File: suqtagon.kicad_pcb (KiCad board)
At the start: 2 copper layers, 100 x 86.6 mm, 2 parts

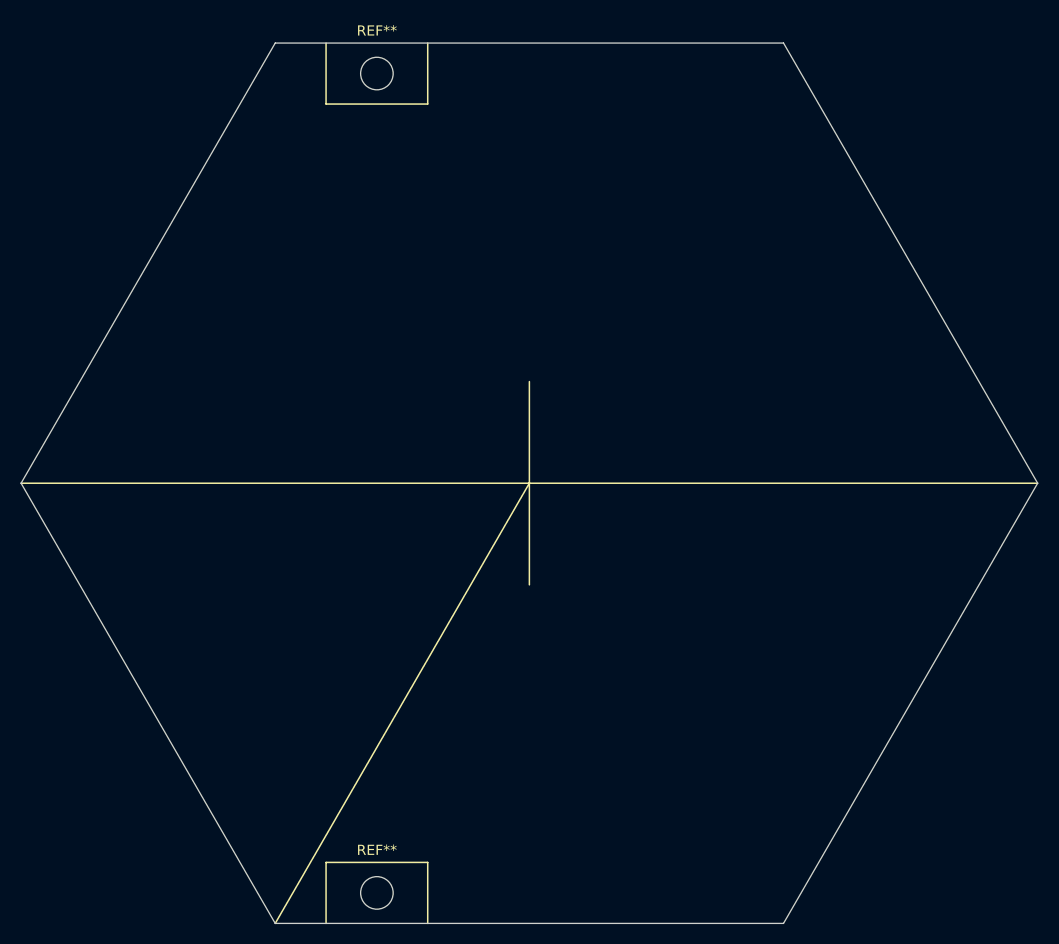
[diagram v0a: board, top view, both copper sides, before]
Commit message: addded some mount holes
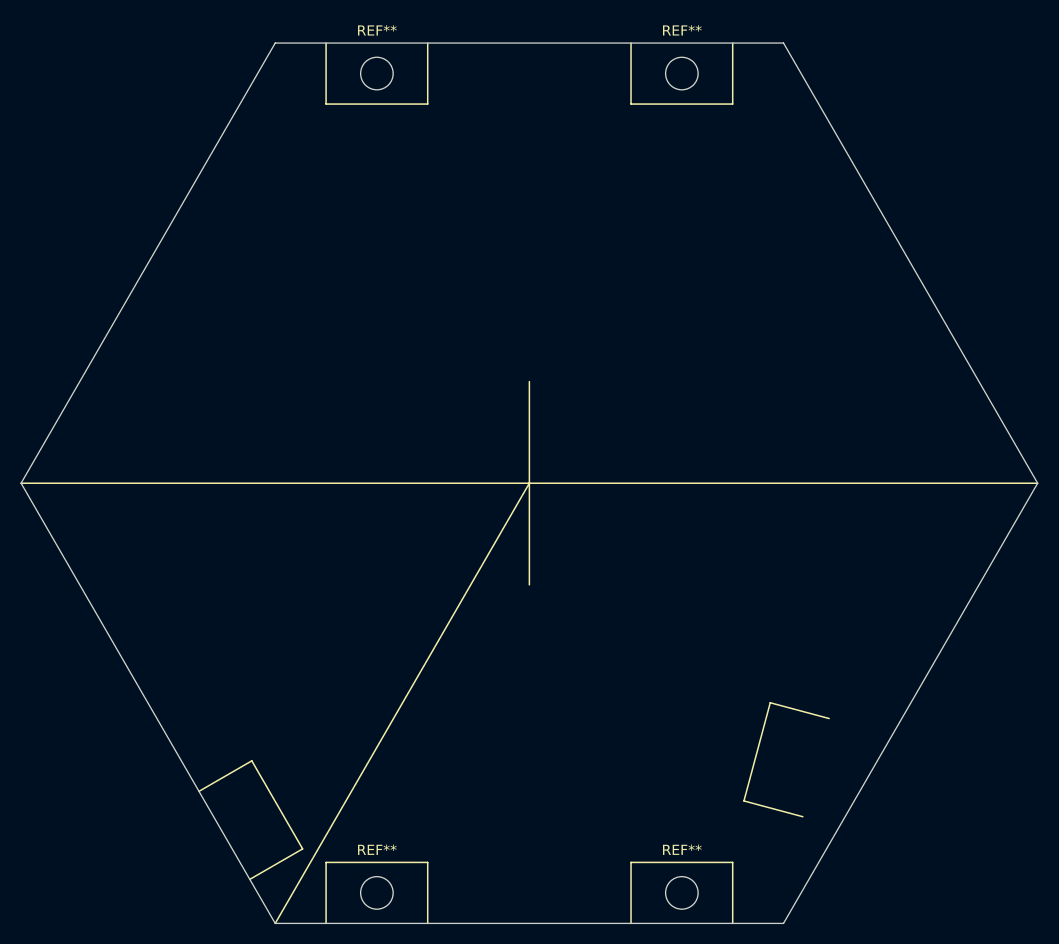
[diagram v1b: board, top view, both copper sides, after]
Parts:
- added REF**: MountingHole_3.2mm_M3, MountingHole:MountingHole_3.2mm_M3, F.Cu at (115.0, 53.0)
- added REF**: MountingHole_3.2mm_M3, MountingHole:MountingHole_3.2mm_M3, F.Cu at (115.0, 133.6)
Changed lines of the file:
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@@
   (net 0 "")
   (footprint "MountingHole:MountingHole_3.2mm_M3" (layer "F.Cu")
+    (at 115 53)
+    (descr "Mounting Hole 3.2mm, no annular, M3")
+    (tags "mounting hole 3.2mm no annular m3")
+    (attr exclude_from_pos_files exclude_from_bom)
+    (fp_text reference "REF**" (at 0 -4.2) (layer "F.SilkS")
+      (effects (font (size 1 1) (thickness 0.15)))
+    )
+    (fp_text value "MountingHole_3.2mm_M3" (at 0 4.2) (layer "F.Fab")
+      (effects (font (size 1 1) (thickness 0.15)))
+    )
+    (fp_text user "${REFERENCE}" (at 0 0) (layer "F.Fab")
+      (effects (font (size 1 1) (thickness 0.15)))
+    )
+    (fp_circle (center 0 0) (end 3.2 0) (layer "Cmts.User") (width 0.15) (fill none))
+    (fp_circle (center 0 0) (end 3.45 0) (layer "F.CrtYd") (width 0.05) (fill none))
+    (pad "" np_thru_hole circle (at 0 0) (size 3.2 3.2) (drill 3.2) (layers *.Cu *.Mask))
+  )
+  (footprint "MountingHole:MountingHole_3.2mm_M3" (layer "F.Cu")
     (at 85 133.6)
+    (descr "Mounting Hole 3.2mm, no annular, M3")
+    (tags "mounting hole 3.2mm no annular m3")
+    (attr exclude_from_pos_files exclude_from_bom)
+    (fp_text reference "REF**" (at 0 -4.2) (layer "F.SilkS")
+      (effects (font (size 1 1) (thickness 0.15)))
+    )
+    (fp_text value "MountingHole_3.2mm_M3" (at 0 4.2) (layer "F.Fab")
+      (effects (font (size 1 1) (thickness 0.15)))
+    )
+    (fp_text user "${REFERENCE}" (at 0 0) (layer "F.Fab")
+      (effects (font (size 1 1) (thickness 0.15)))
+    )
+    (fp_circle (center 0 0) (end 3.2 0) (layer "Cmts.User") (width 0.15) (fill none))
+    (fp_circle (center 0 0) (end 3.45 0) (layer "F.CrtYd") (width 0.05) (fill none))
+    (pad "" np_thru_hole circle (at 0 0) (size 3.2 3.2) (drill 3.2) (layers *.Cu *.Mask))
+  )
+  (footprint "MountingHole:MountingHole_3.2mm_M3" (layer "F.Cu")
+    (at 115 133.6)
     (descr "Mounting Hole 3.2mm, no annular, M3")
     (tags "mounting hole 3.2mm no annular m3")
@@
     (pad "" np_thru_hole circle (at 0 0) (size 3.2 3.2) (drill 3.2) (layers *.Cu *.Mask))
   )
+  (gr_line (start 121.107866 124.554275) (end 123.695876 114.895197) (layer "F.SilkS") (width 0.15))
+  (gr_line (start 129.491324 116.448003) (end 123.695876 114.895197) (layer "F.SilkS") (width 0.15))
   (gr_line (start 100 83.3) (end 100 103.3) (layer "F.SilkS") (width 0.15))
   (gr_line (start 90 56) (end 90 50) (layer "F.SilkS") (width 0.15))
   (gr_line (start 50 93.3) (end 150 93.3) (layer "F.SilkS") (width 0.15))
   (gr_line (start 80 136.6) (end 80 130.6) (layer "F.SilkS") (width 0.15))
+  (gr_line (start 126.903313 126.107082) (end 121.107866 124.554275) (layer "F.SilkS") (width 0.15))
+  (gr_line (start 110 56) (end 120 56) (layer "F.SilkS") (width 0.15))
+  (gr_line (start 72.696 120.61) (end 77.696 129.27) (layer "F.SilkS") (width 0.15))
   (gr_line (start 80 56) (end 90 56) (layer "F.SilkS") (width 0.15))
+  (gr_line (start 110 56) (end 110 50) (layer "F.SilkS") (width 0.15))
+  (gr_line (start 67.5 123.61) (end 72.696 120.61) (layer "F.SilkS") (width 0.15))
+  (gr_line (start 110 130.6) (end 120 130.6) (layer "F.SilkS") (width 0.15))
   (gr_line (start 80 130.6) (end 90 130.6) (layer "F.SilkS") (width 0.15))
   (gr_line (start 75 136.6) (end 100 93.3) (layer "F.SilkS") (width 0.15))
+  (gr_line (start 120 136.6) (end 120 130.6) (layer "F.SilkS") (width 0.15))
+  (gr_line (start 120 56) (end 120 50) (layer "F.SilkS") (width 0.15))
+  (gr_line (start 72.5 132.27) (end 77.696 129.27) (layer "F.SilkS") (width 0.15))
   (gr_line (start 90 136.6) (end 90 130.6) (layer "F.SilkS") (width 0.15))
   (gr_line (start 80 56) (end 80 50) (layer "F.SilkS") (width 0.15))
+  (gr_line (start 110 136.6) (end 110 130.6) (layer "F.SilkS") (width 0.15))
   (gr_line (start 75 50) (end 125 50) (layer "Edge.Cuts") (width 0.1))
   (gr_line (start 125 136.6) (end 150 93.3) (layer "Edge.Cuts") (width 0.1))

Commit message: more mounting holes
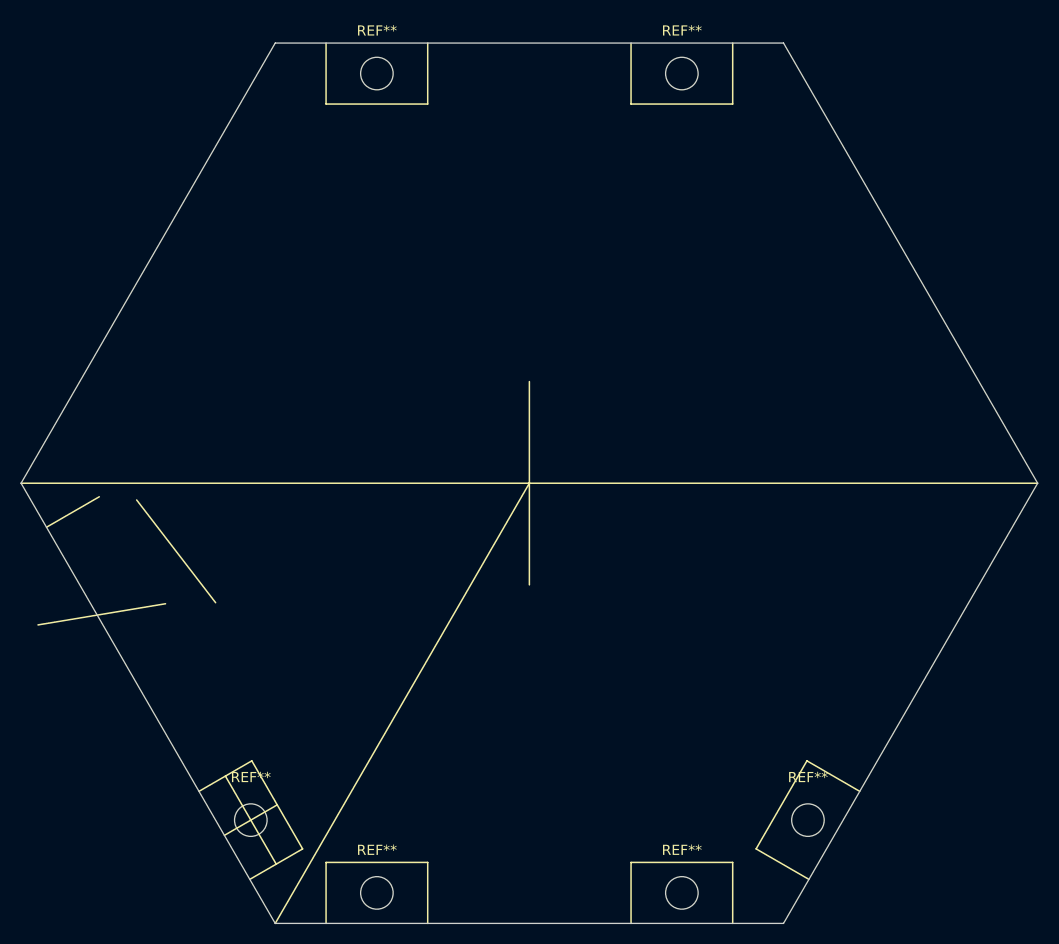
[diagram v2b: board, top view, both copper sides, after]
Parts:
- added REF**: MountingHole_3.2mm_M3, MountingHole:MountingHole_3.2mm_M3, F.Cu at (72.6, 126.4)
- added REF**: MountingHole_3.2mm_M3, MountingHole:MountingHole_3.2mm_M3, F.Cu at (127.4, 126.4)
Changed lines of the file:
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@@
+  )
+  (footprint "MountingHole:MountingHole_3.2mm_M3" (layer "F.Cu")
+    (at 72.598 126.44)
+    (descr "Mounting Hole 3.2mm, no annular, M3")
+    (tags "mounting hole 3.2mm no annular m3")
+    (attr exclude_from_pos_files exclude_from_bom)
+    (fp_text reference "REF**" (at 0 -4.2) (layer "F.SilkS")
+      (effects (font (size 1 1) (thickness 0.15)))
+    )
+    (fp_text value "MountingHole_3.2mm_M3" (at 0 4.2) (layer "F.Fab")
+      (effects (font (size 1 1) (thickness 0.15)))
+    )
+    (fp_text user "${REFERENCE}" (at 0 0) (layer "F.Fab")
+      (effects (font (size 1 1) (thickness 0.15)))
+    )
+    (fp_circle (center 0 0) (end 3.2 0) (layer "Cmts.User") (width 0.15) (fill none))
+    (fp_circle (center 0 0) (end 3.45 0) (layer "F.CrtYd") (width 0.05) (fill none))
+    (pad "" np_thru_hole circle (at 0 0) (size 3.2 3.2) (drill 3.2) (layers *.Cu *.Mask))
   )
   (footprint "MountingHole:MountingHole_3.2mm_M3" (layer "F.Cu")
@@
     (pad "" np_thru_hole circle (at 0 0) (size 3.2 3.2) (drill 3.2) (layers *.Cu *.Mask))
   )
-  (gr_line (start 121.107866 124.554275) (end 123.695876 114.895197) (layer "F.SilkS") (width 0.15))
-  (gr_line (start 129.491324 116.448003) (end 123.695876 114.895197) (layer "F.SilkS") (width 0.15))
+  (footprint "MountingHole:MountingHole_3.2mm_M3" (layer "F.Cu")
+    (at 127.402 126.44)
+    (descr "Mounting Hole 3.2mm, no annular, M3")
+    (tags "mounting hole 3.2mm no annular m3")
+    (attr exclude_from_pos_files exclude_from_bom)
+    (fp_text reference "REF**" (at 0 -4.2) (layer "F.SilkS")
+      (effects (font (size 1 1) (thickness 0.15)))
+    )
+    (fp_text value "MountingHole_3.2mm_M3" (at 0 4.2) (layer "F.Fab")
+      (effects (font (size 1 1) (thickness 0.15)))
+    )
+    (fp_text user "${REFERENCE}" (at 0 0) (layer "F.Fab")
+      (effects (font (size 1 1) (thickness 0.15)))
+    )
+    (fp_circle (center 0 0) (end 3.2 0) (layer "Cmts.User") (width 0.15) (fill none))
+    (fp_circle (center 0 0) (end 3.45 0) (layer "F.CrtYd") (width 0.05) (fill none))
+    (pad "" np_thru_hole circle (at 0 0) (size 3.2 3.2) (drill 3.2) (layers *.Cu *.Mask))
+  )
+  (gr_line (start 127.304 120.61) (end 122.304 129.27) (layer "F.SilkS") (width 0.15))
+  (gr_line (start 51.6636 107.2388) (end 64.2112 105.156) (layer "F.SilkS") (width 0.15))
+  (gr_line (start 132.5 123.61) (end 127.304 120.61) (layer "F.SilkS") (width 0.15))
   (gr_line (start 100 83.3) (end 100 103.3) (layer "F.SilkS") (width 0.15))
+  (gr_line (start 61.3664 94.9452) (end 69.1388 105.0544) (layer "F.SilkS") (width 0.15))
   (gr_line (start 90 56) (end 90 50) (layer "F.SilkS") (width 0.15))
   (gr_line (start 50 93.3) (end 150 93.3) (layer "F.SilkS") (width 0.15))
   (gr_line (start 80 136.6) (end 80 130.6) (layer "F.SilkS") (width 0.15))
-  (gr_line (start 126.903313 126.107082) (end 121.107866 124.554275) (layer "F.SilkS") (width 0.15))
+  (gr_line (start 127.5 132.27) (end 122.304 129.27) (layer "F.SilkS") (width 0.15))
   (gr_line (start 110 56) (end 120 56) (layer "F.SilkS") (width 0.15))
+  (gr_line (start 70 127.94) (end 75.196 124.94) (layer "F.SilkS") (width 0.15))
   (gr_line (start 72.696 120.61) (end 77.696 129.27) (layer "F.SilkS") (width 0.15))
   (gr_line (start 80 56) (end 90 56) (layer "F.SilkS") (width 0.15))
+  (gr_line (start 52.5 97.63) (end 57.696 94.63) (layer "F.SilkS") (width 0.15))
   (gr_line (start 110 56) (end 110 50) (layer "F.SilkS") (width 0.15))
   (gr_line (start 67.5 123.61) (end 72.696 120.61) (layer "F.SilkS") (width 0.15))
+  (gr_line (start 70.098 122.11) (end 75.098 130.77) (layer "F.SilkS") (width 0.15))
   (gr_line (start 110 130.6) (end 120 130.6) (layer "F.SilkS") (width 0.15))
   (gr_line (start 80 130.6) (end 90 130.6) (layer "F.SilkS") (width 0.15))
